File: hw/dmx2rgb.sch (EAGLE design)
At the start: 45 parts, among them IC1 ATMEGA88-20A, IC2 7805

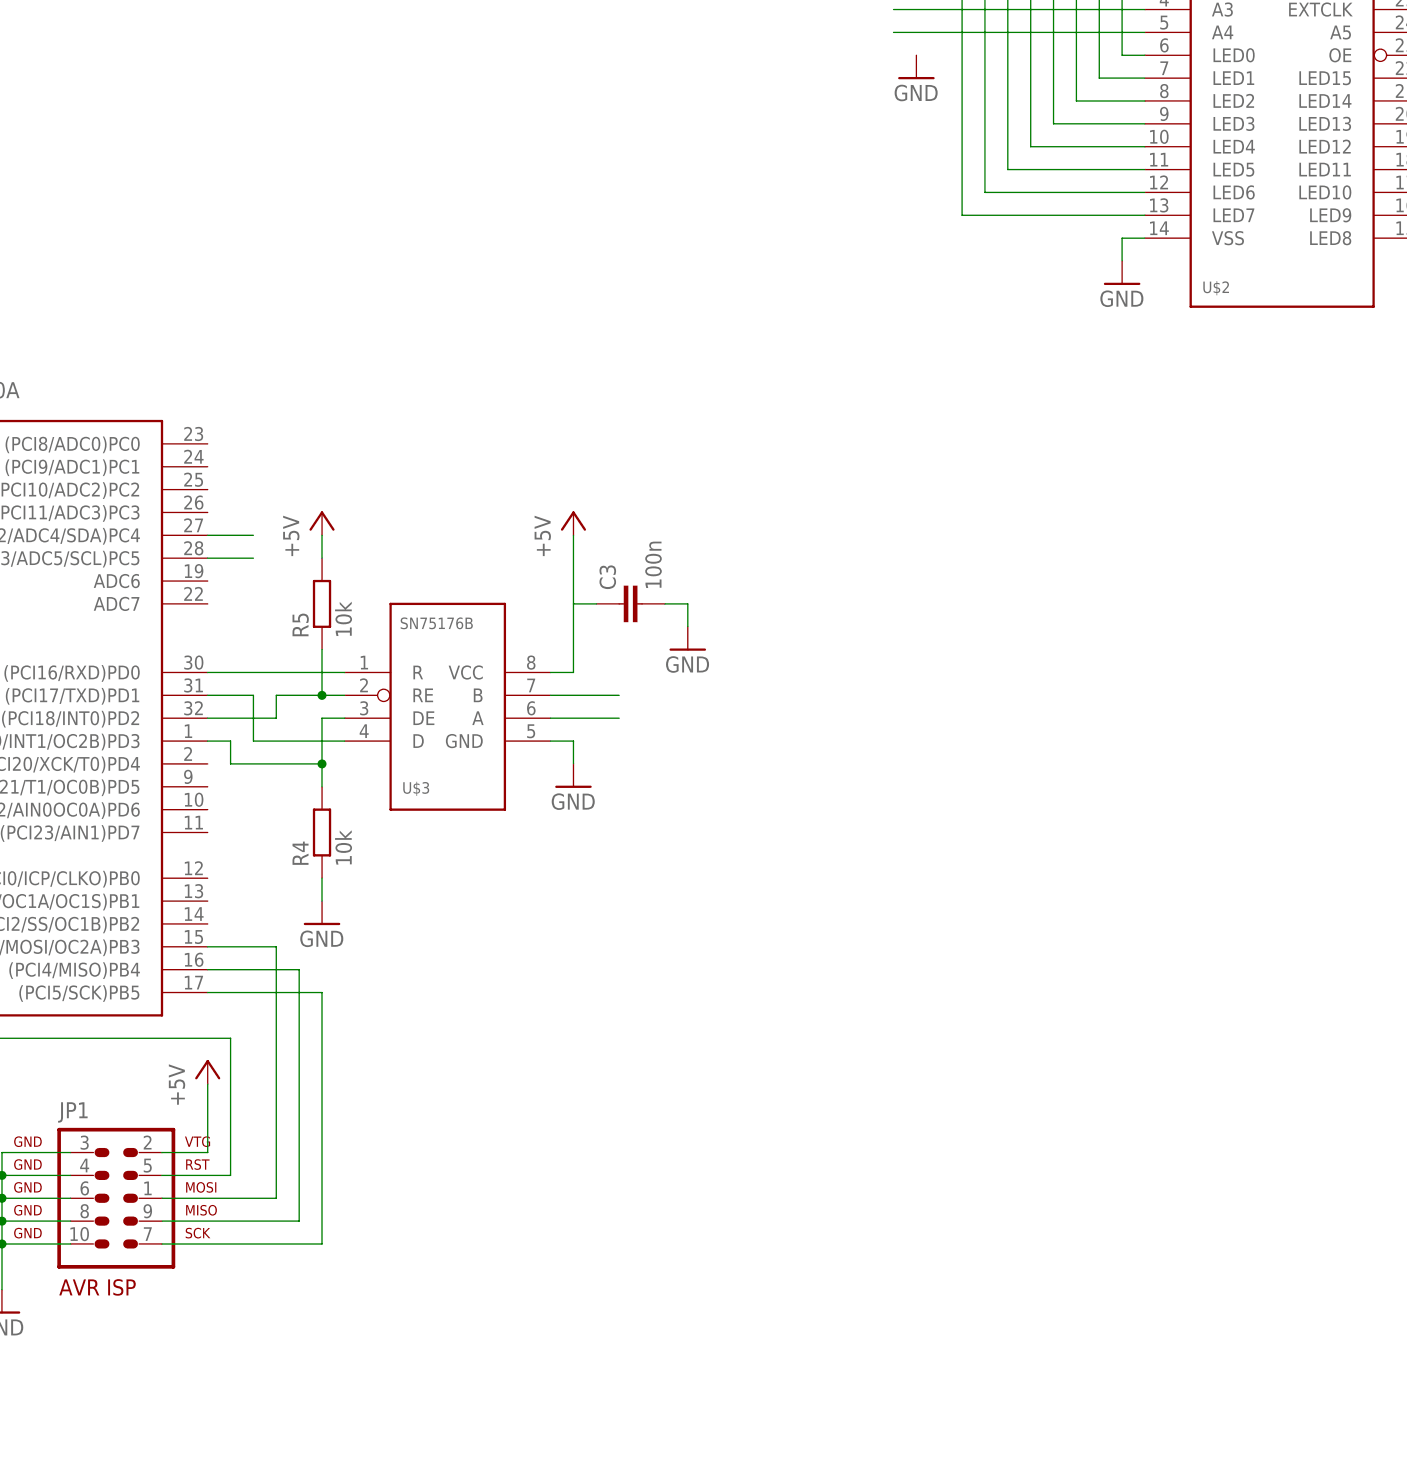
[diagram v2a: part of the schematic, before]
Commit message: adressing through solder jumpers
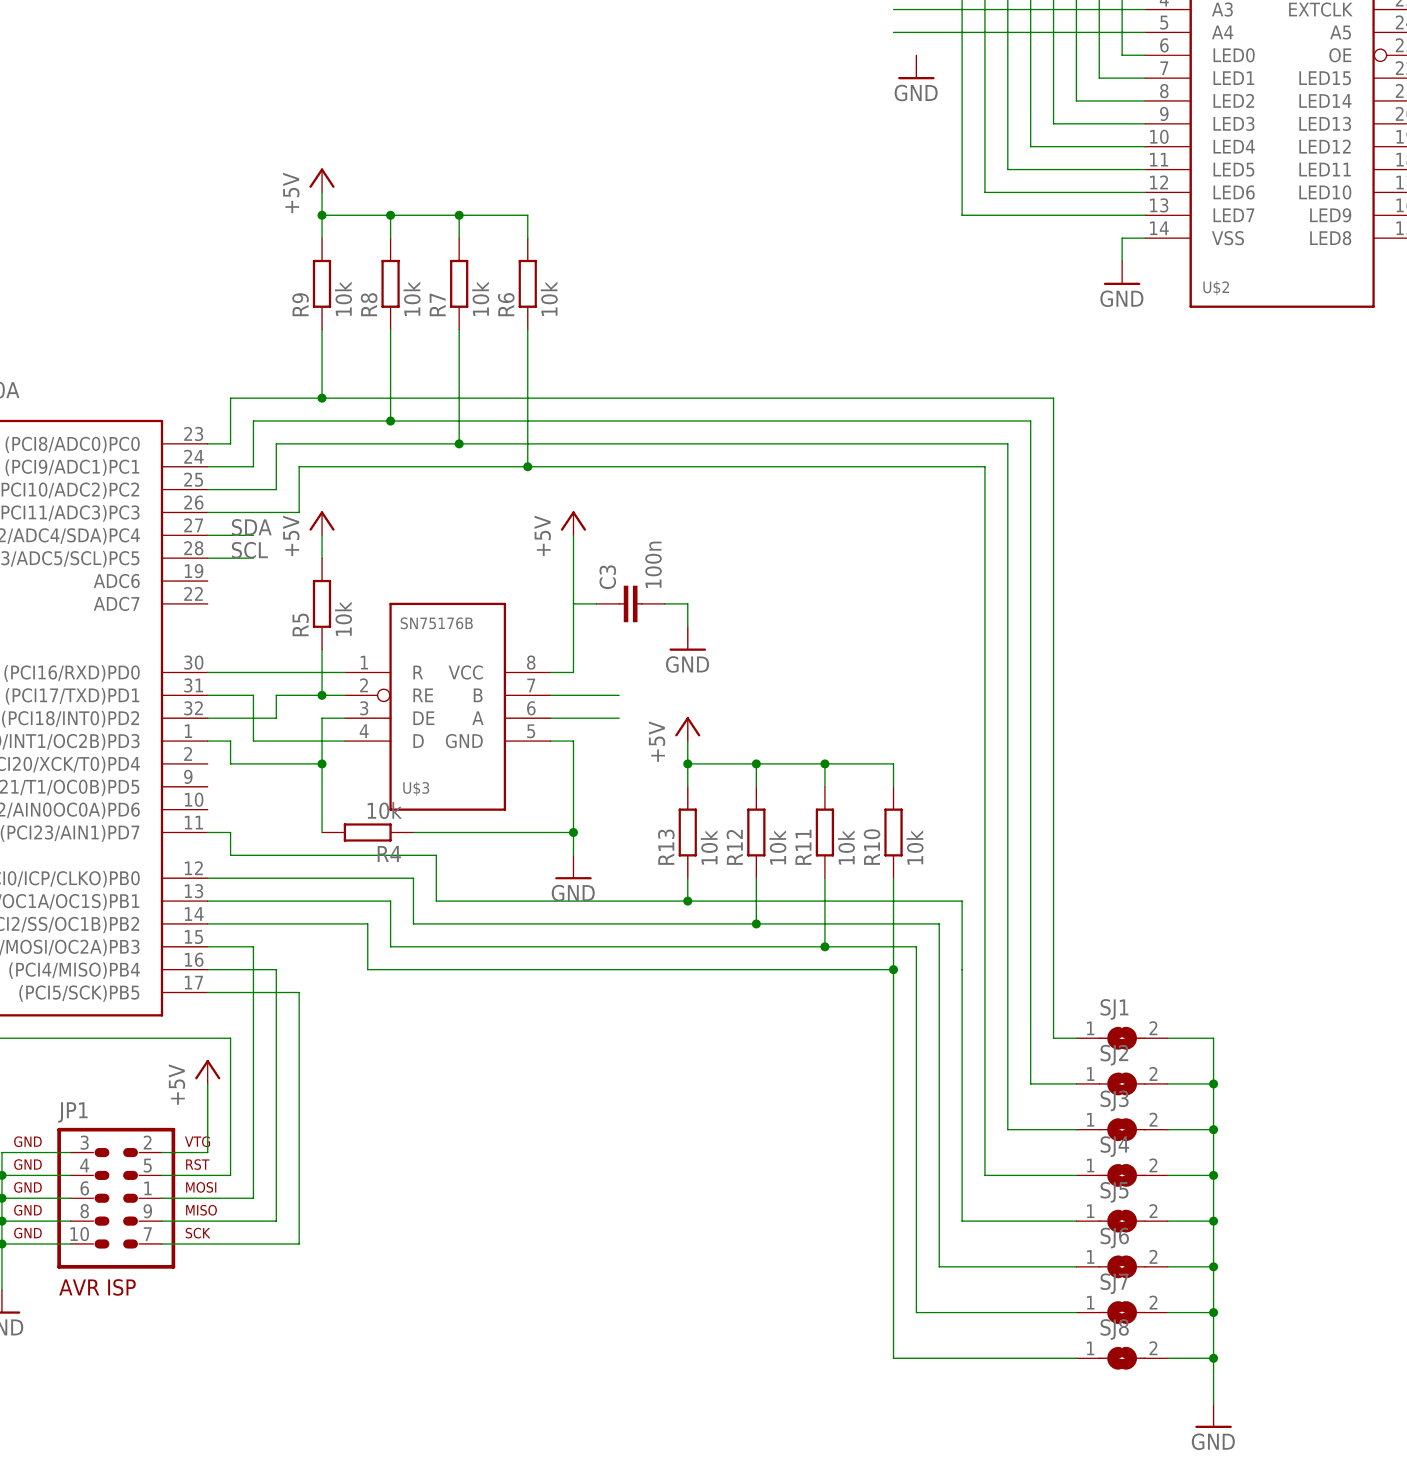
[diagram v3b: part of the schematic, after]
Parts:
- added R10, R11, R12, R13, R6, R7, R8, R9: 10k, dmx2rgb:R0805
- added SJ1, SJ2, SJ3, SJ4, SJ5, SJ6, SJ7, SJ8: (no value), dmx2rgb:SJ
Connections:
- new net N$35: IC1.(PCI11/ADC3)PC3, R6.1, SJ4.1
- new net N$36: IC1.(PCI10/ADC2)PC2, R7.1, SJ3.1
- new net N$39: IC1.(PCI9/ADC1)PC1, R8.1, SJ2.1
- new net N$40: IC1.(PCI8/ADC0)PC0, R9.1, SJ1.1
- new net N$43: IC1.(PCI23/AIN1)PD7, R13.1
- new net N$44: IC1.(PCI0/ICP/CLKO)PB0, R12.1, SJ6.1
- new net N$45: IC1.(PCI1/OC1A/OC1S)PB1, R11.1, SJ7.1
- new net N$46: IC1.(PCI2/SS/OC1B)PB2, R10.1, SJ8.1
- new net N$62: SJ5.1
- net +5V: now also R10.2, R11.2, R12.2, R13.2, R6.2, R7.2, R8.2, R9.2
- net GND: now also SJ1.2, SJ2.2, SJ3.2, SJ4.2, SJ5.2, SJ6.2, SJ7.2, SJ8.2
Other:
- moved on the sheet: R4

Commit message: all parts added some parts placed
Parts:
- removed R10, R11, R12, R13, R9: 10k, dmx2rgb:R0805
- added C11, C12: 100n, dmx2rgb:C0805
- added LED1, LED2, LED3: (no value), dmx2rgb:LEDCHIPLED_0805
- added PAD100, PAD17, PAD18, PAD19, PAD20, PAD21, PAD22, PAD23, PAD24, PAD25, PAD26, PAD27, PAD28, PAD29, PAD30, PAD31, PAD32, PAD33, PAD34, PAD35, PAD36, PAD37, PAD38, PAD39, PAD40, PAD41, PAD42, PAD43, PAD44, PAD45, PAD46, PAD47, PAD48, PAD49, PAD50, PAD51, PAD52, PAD53, PAD54, PAD55, PAD56, PAD57, PAD58, PAD59, PAD60, PAD61, PAD62, PAD63, PAD64, PAD65, PAD66, PAD67, PAD68, PAD69, PAD70, PAD71, PAD72, PAD73, PAD74, PAD75, PAD76, PAD77, PAD78, PAD79, PAD80, PAD81, PAD82, PAD83, PAD84, PAD85, PAD86, PAD87, PAD88, PAD89, PAD90, PAD91, PAD92, PAD93, PAD94, PAD95, PAD96, PAD99: (no value), dmx2rgb:SMD_PAD_LONG
- added PAD97, PAD98: (no value), dmx2rgb:SMD5
- added U$11, U$13, U$14, U$15, U$16, U$17, U$18, U$19, U$20, U$22, U$23, U$24, U$25, U$26, U$27, U$28: IRF7303, dmx2rgb:IRF7303
- added U$12, U$21: PCA9685, dmx2rgb:PCA9685
- PAD1, PAD10, PAD11, PAD12, PAD13, PAD14, PAD15, PAD16, PAD2, PAD3, PAD4, PAD5, PAD6, PAD7, PAD8, PAD9: device dmx2rgb:PAD_THT_1.6 -> dmx2rgb:SMD_PAD_LONG
- R6, R7, R8: value 10k -> (none)
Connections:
- removed net N$12: U$3.A
- removed net N$62: SJ5.1
- new net LED_ENABLE: IC1.(PCI19/INT1/OC2B)PD3, R5.1, U$12.OE, U$2.OE, U$21.OE
- new net N$100: PAD35.P, U$22.D1A, U$22.D1B
- new net N$101: PAD36.P, U$22.D2A, U$22.D2B
- new net N$102: U$21.LED4, U$22.G2
- new net N$103: PAD37.P, U$23.D1A, U$23.D1B
- new net N$104: PAD38.P, U$23.D2A, U$23.D2B
- new net N$105: U$21.LED3, U$23.G1
- new net N$106: U$21.LED2, U$23.G2
- new net N$107: PAD39.P, U$24.D1A, U$24.D1B
- new net N$108: PAD40.P, U$24.D2A, U$24.D2B
- new net N$109: U$21.LED1, U$24.G1
- new net N$110: U$21.LED0, U$24.G2
- new net N$111: PAD41.P, U$25.D1A, U$25.D1B
- new net N$112: PAD42.P, U$25.D2A, U$25.D2B
- new net N$113: PAD43.P, U$26.D1A, U$26.D1B
- new net N$114: PAD44.P, U$26.D2A, U$26.D2B
- new net N$115: PAD45.P, U$27.D1A, U$27.D1B
- new net N$116: PAD46.P, U$27.D2A, U$27.D2B
- new net N$117: PAD47.P, U$28.D1A, U$28.D1B
- new net N$118: PAD48.P, U$28.D2A, U$28.D2B
- new net N$119: U$20.G1, U$21.LED7
- new net N$120: U$20.G2, U$21.LED6
- new net N$121: U$21.LED5, U$22.G1
- new net N$122: U$21.LED8, U$25.G1
- new net N$123: U$21.LED9, U$25.G2
- new net N$124: U$21.LED10, U$26.G1
- new net N$125: U$21.LED11, U$26.G2
- new net N$126: U$21.LED12, U$27.G1
- new net N$127: U$21.LED13, U$27.G2
- new net N$128: U$21.LED14, U$28.G1
- new net N$129: U$21.LED15, U$28.G2
- new net N$47: PAD100.P, U$3.A
- new net N$48: PAD17.P, U$11.D1A, U$11.D1B
- new net N$49: PAD18.P, U$11.D2A, U$11.D2B
- new net N$61: PAD19.P, U$13.D1A, U$13.D1B
- new net N$63: PAD20.P, U$13.D2A, U$13.D2B
- new net N$64: U$12.LED4, U$13.G2
- new net N$65: PAD21.P, U$14.D1A, U$14.D1B
- new net N$66: PAD22.P, U$14.D2A, U$14.D2B
- new net N$67: U$12.LED3, U$14.G1
- new net N$68: U$12.LED2, U$14.G2
- new net N$69: PAD23.P, U$15.D1A, U$15.D1B
- new net N$70: PAD24.P, U$15.D2A, U$15.D2B
- new net N$71: U$12.LED1, U$15.G1
- new net N$72: U$12.LED0, U$15.G2
- new net N$73: PAD25.P, U$16.D1A, U$16.D1B
- new net N$74: PAD26.P, U$16.D2A, U$16.D2B
- new net N$75: PAD27.P, U$17.D1A, U$17.D1B
- new net N$76: PAD28.P, U$17.D2A, U$17.D2B
- new net N$77: PAD29.P, U$18.D1A, U$18.D1B
- new net N$78: PAD30.P, U$18.D2A, U$18.D2B
- new net N$79: PAD31.P, U$19.D1A, U$19.D1B
- new net N$80: PAD32.P, U$19.D2A, U$19.D2B
- new net N$81: U$11.G1, U$12.LED7
- new net N$82: U$11.G2, U$12.LED6
- new net N$83: U$12.LED5, U$13.G1
- new net N$84: U$12.LED8, U$16.G1
- new net N$85: U$12.LED9, U$16.G2
- new net N$86: U$12.LED10, U$17.G1
- new net N$87: U$12.LED11, U$17.G2
- new net N$88: U$12.LED12, U$18.G1
- new net N$89: U$12.LED13, U$18.G2
- new net N$90: U$12.LED14, U$19.G1
- new net N$91: U$12.LED15, U$19.G2
- new net N$98: PAD33.P, U$20.D1A, U$20.D1B
- new net N$99: PAD34.P, U$20.D2A, U$20.D2B
- net +12V: now also PAD49.P, PAD50.P, PAD51.P, PAD52.P, PAD53.P, PAD54.P, PAD55.P, PAD56.P, PAD57.P, PAD58.P, PAD59.P, PAD60.P, PAD61.P, PAD62.P, PAD63.P, PAD64.P, PAD65.P, PAD66.P, PAD67.P, PAD68.P, PAD69.P, PAD70.P, PAD71.P, PAD72.P, PAD73.P, PAD74.P, PAD75.P, PAD76.P, PAD77.P, PAD78.P, PAD79.P, PAD80.P, PAD81.P, PAD82.P, PAD83.P, PAD84.P, PAD85.P, PAD86.P, PAD87.P, PAD88.P, PAD89.P, PAD90.P, PAD91.P, PAD92.P, PAD93.P, PAD94.P, PAD95.P, PAD96.P, PAD97.P
- net +5V: now also C11.2, C12.2, LED1.A, LED2.A, LED3.A, U$12.A0, U$12.A1, U$12.VDD, U$2.A0, U$21.A0, U$21.A1, U$21.A2, U$21.VDD; no longer R10.2, R11.2, R12.2, R13.2, R6.2, R7.2, R8.2, R9.2
- net GND: now also C11.1, C12.1, PAD98.P, U$11.S1, U$11.S2, U$12.A2, U$12.A3, U$12.A4, U$12.A5, U$12.EXTCLK, U$12.VSS, U$13.S1, U$13.S2, U$14.S1, U$14.S2, U$15.S1, U$15.S2, U$16.S1, U$16.S2, U$17.S1, U$17.S2, U$18.S1, U$18.S2, U$19.S1, U$19.S2, U$2.A1, U$2.A2, U$2.A3, U$2.A4, U$20.S1, U$20.S2, U$21.A3, U$21.A4, U$21.A5, U$21.EXTCLK, U$21.VSS, U$22.S1, U$22.S2, U$23.S1, U$23.S2, U$24.S1, U$24.S2, U$25.S1, U$25.S2, U$26.S1, U$26.S2, U$27.S1, U$27.S2, U$28.S1, U$28.S2
- net N$11: now also PAD99.P
- net N$15: now also LED2.C, R7.2; no longer U$2.A0
- net N$27: now also LED1.C, R6.2; no longer U$2.A1
- net N$28: now also IC1.(PCI0/ICP/CLKO)PB0, R6.1; no longer U$2.A2
- net N$3: now also LED3.C, R8.2; no longer IC1.(PCI18/INT0)PD2, R5.1, U$3.RE
- net N$31: now also IC1.(PCI1/OC1A/OC1S)PB1, R7.1; no longer U$2.A3
- net N$32: now also IC1.(PCI2/SS/OC1B)PB2, R8.1; no longer U$2.A4
- net N$35: no longer R6.1
- net N$36: no longer R7.1
- net N$39: no longer R8.1
- net N$4: now also IC1.(PCI18/INT0)PD2, U$3.RE; no longer IC1.(PCI19/INT1/OC2B)PD3
- net N$40: no longer R9.1
- net N$43: now also IC1.(PCI20/XCK/T0)PD4, SJ5.1; no longer IC1.(PCI23/AIN1)PD7, R13.1
- net N$44: now also IC1.(PCI21/T1/OC0B)PD5; no longer IC1.(PCI0/ICP/CLKO)PB0, R12.1
- net N$45: now also IC1.(PCI22/AIN0OC0A)PD6; no longer IC1.(PCI1/OC1A/OC1S)PB1, R11.1
- net N$46: now also IC1.(PCI23/AIN1)PD7; no longer IC1.(PCI2/SS/OC1B)PB2, R10.1
- net SCL: now also U$12.SCL, U$21.SCL
- net SDA: now also U$12.SDA, U$21.SDA
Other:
- moved on the sheet: C3, C6, PAD1, PAD10, PAD11, PAD12, PAD13, PAD14, PAD15, PAD16, PAD2, PAD3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
